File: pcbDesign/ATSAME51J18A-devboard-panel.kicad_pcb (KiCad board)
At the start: 2 copper layers, 100 x 100 mm, 294 parts, among them J1 Micro_SD_Card, J10 CAN, J11 Conn_01x32_Male, J2 BAT, J3 QWIIC, J7 Conn_01x32_Male, J9 USB4105_REVA, SW1 RST, U1 TCAN1051GVDRQ1, U2 ATSAME51J18A-A, U3 MIC5219-5.0YMM, U4 LM27762, U5 LM2775QDSGTQ1, U6 SC630AULTRT, U7 BQ24074RGT, U8 BQ27441DRZR-G1B, Y1 32.768

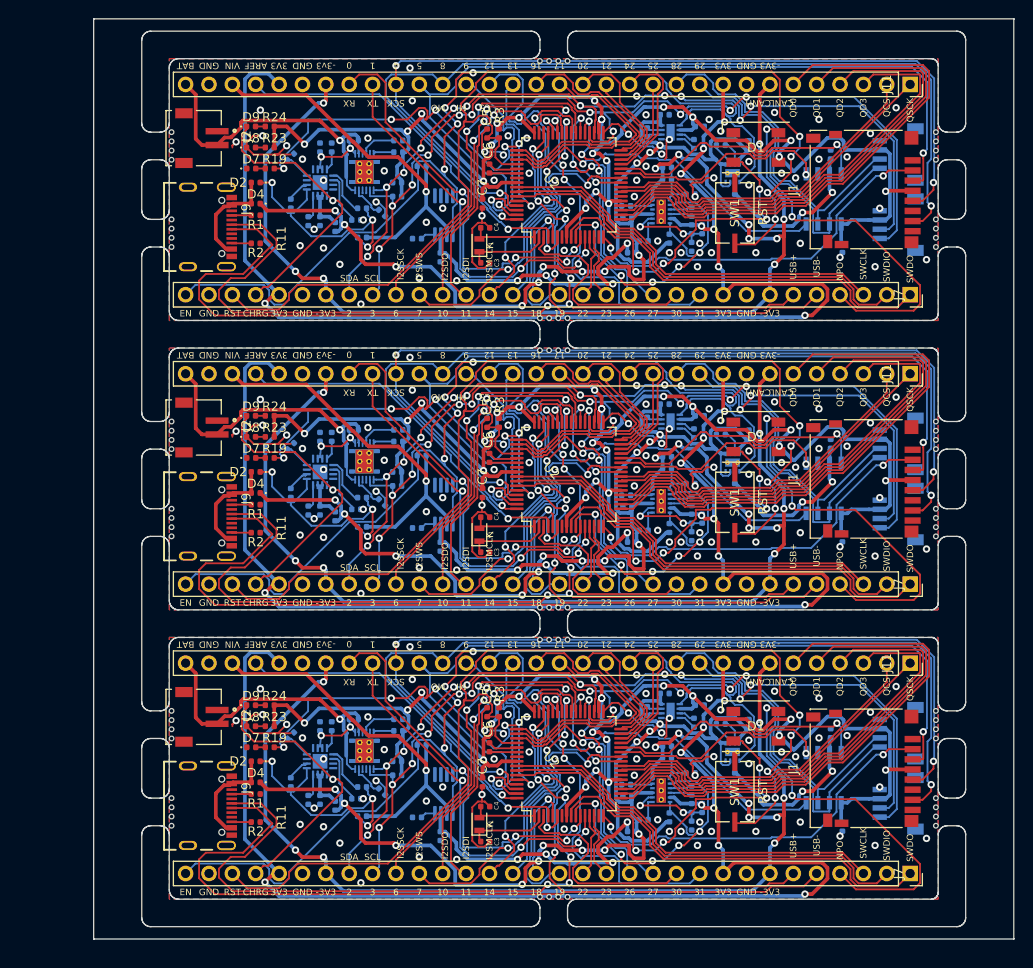
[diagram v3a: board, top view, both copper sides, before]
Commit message: Fixed panelizing issues
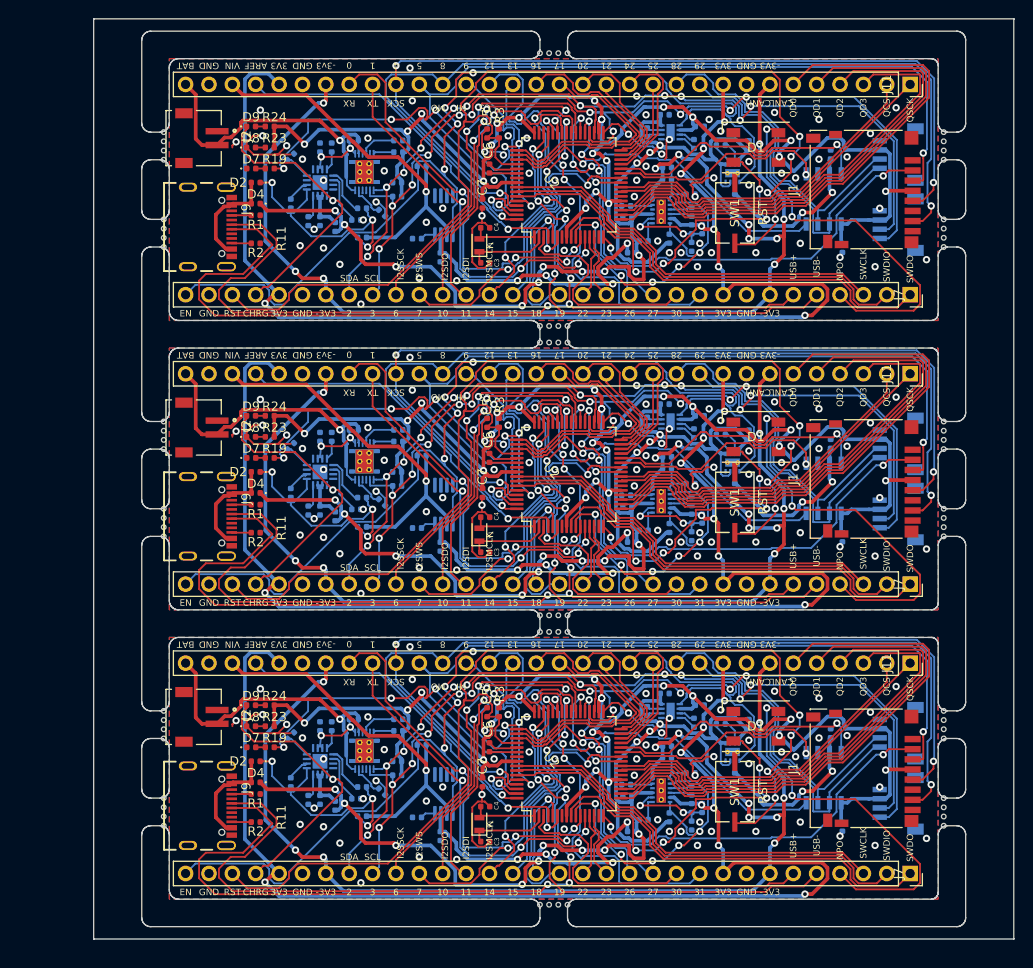
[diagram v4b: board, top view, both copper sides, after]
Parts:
- removed the D9 at (58.9, 120.3)
- removed the D9 at (58.9, 88.8)
- removed the D9 at (58.9, 57.4)
- removed the R24 at (60.9, 120.3)
- removed the R24 at (60.9, 88.8)
- removed the R24 at (60.9, 57.4)
- removed the REF** at (133.3, 133.4)
- removed the REF** at (50.2, 131.4)
- removed the REF** at (50.2, 132.4)
- removed the REF** at (50.2, 133.4)
- removed the REF** at (50.2, 120.9)
- removed the REF** at (50.2, 121.9)
- removed the REF** at (50.2, 122.9)
- removed the REF** at (50.2, 123.9)
- removed the REF** at (133.3, 101.9)
- removed the REF** at (133.3, 100.9)
- removed the REF** at (133.3, 99.9)
- removed the REF** at (133.3, 132.4)
- removed the REF** at (133.3, 98.9)
- removed the REF** at (133.3, 92.4)
- removed the REF** at (133.3, 91.4)
- removed the REF** at (133.3, 90.4)
- removed the REF** at (133.3, 89.4)
- removed the REF** at (50.2, 98.9)
- removed the REF** at (50.2, 99.9)
- removed the REF** at (50.2, 100.9)
- removed the REF** at (50.2, 101.9)
- removed the REF** at (50.2, 89.4)
- removed the REF** at (133.3, 131.4)
- removed the REF** at (50.2, 90.4)
- removed the REF** at (50.2, 91.4)
- removed the REF** at (50.2, 92.4)
- removed the REF** at (133.3, 70.5)
- removed the REF** at (133.3, 69.5)
- removed the REF** at (133.3, 68.5)
- removed the REF** at (133.3, 67.5)
- removed the REF** at (133.3, 61.0)
- removed the REF** at (133.3, 60.0)
- removed the REF** at (133.3, 59.0)
- removed the REF** at (133.3, 130.4)
- removed the REF** at (133.3, 58.0)
- removed the REF** at (50.2, 67.5)
- removed the REF** at (50.2, 68.5)
- removed the REF** at (50.2, 69.5)
- removed the REF** at (50.2, 70.5)
- removed the REF** at (50.2, 58.0)
- removed the REF** at (50.2, 59.0)
- removed the REF** at (50.2, 60.0)
- removed the REF** at (50.2, 61.0)
- removed the REF** at (90.3, 141.1)
- removed the REF** at (133.3, 123.9)
- removed the REF** at (91.3, 141.1)
- removed the REF** at (92.3, 141.1)
- removed the REF** at (93.3, 141.1)
- removed the REF** at (93.3, 113.1)
- removed the REF** at (92.3, 113.1)
- removed the REF** at (91.3, 113.1)
- removed the REF** at (90.3, 113.1)
- removed the REF** at (90.3, 109.6)
- removed the REF** at (91.3, 109.6)
- removed the REF** at (92.3, 109.6)
- removed the REF** at (133.3, 122.9)
- removed the REF** at (93.3, 109.6)
- removed the REF** at (93.3, 81.7)
- removed the REF** at (92.3, 81.7)
- removed the REF** at (91.3, 81.7)
- removed the REF** at (90.3, 81.7)
- removed the REF** at (90.3, 78.2)
- removed the REF** at (91.3, 78.2)
- removed the REF** at (92.3, 78.2)
- removed the REF** at (93.3, 78.2)
- removed the REF** at (93.3, 50.2)
- removed the REF** at (133.3, 121.9)
- removed the REF** at (92.3, 50.2)
- removed the REF** at (91.3, 50.2)
- removed the REF** at (90.3, 50.2)
- removed the REF** at (133.3, 120.9)
- removed the REF** at (50.2, 130.4)
- removed the U6 at (104.5, 120.9)
- removed the U6 at (104.5, 89.4)
- removed the U6 at (104.5, 58.0)
- added C23: 4.7u, Capacitor_SMD:C_0402_1005Metric, B.Cu at (66.4, 122.5)
- added C23: 4.7u, Capacitor_SMD:C_0402_1005Metric, B.Cu at (66.4, 91.1)
- added C23: 4.7u, Capacitor_SMD:C_0402_1005Metric, B.Cu at (66.4, 59.7)
- added R1: 5.1k, Resistor_SMD:R_0402_1005Metric, F.Cu at (59.4, 129.9)
- added R1: 5.1k, Resistor_SMD:R_0402_1005Metric, F.Cu at (59.4, 98.5)
- added R1: 5.1k, Resistor_SMD:R_0402_1005Metric, F.Cu at (59.4, 67.0)
- added R2: 5.1k, Resistor_SMD:R_0402_1005Metric, F.Cu at (59.4, 133.0)
- added R2: 5.1k, Resistor_SMD:R_0402_1005Metric, F.Cu at (59.4, 101.5)
- added R2: 5.1k, Resistor_SMD:R_0402_1005Metric, F.Cu at (59.4, 70.1)
- added REF**: NPTH, NPTH, F.Cu at (134.2, 130.4)
- added REF**: NPTH, NPTH, F.Cu at (49.4, 132.4)
- added REF**: NPTH, NPTH, F.Cu at (49.4, 131.4)
- added REF**: NPTH, NPTH, F.Cu at (49.4, 130.4)
- added REF**: NPTH, NPTH, F.Cu at (49.4, 123.9)
- added REF**: NPTH, NPTH, F.Cu at (49.4, 122.9)
- added REF**: NPTH, NPTH, F.Cu at (49.4, 121.9)
- added REF**: NPTH, NPTH, F.Cu at (49.4, 120.9)
- added REF**: NPTH, NPTH, F.Cu at (134.2, 98.9)
- added REF**: NPTH, NPTH, F.Cu at (134.2, 99.9)
- added REF**: NPTH, NPTH, F.Cu at (134.2, 100.9)
- added REF**: NPTH, NPTH, F.Cu at (134.2, 131.4)
- added REF**: NPTH, NPTH, F.Cu at (134.2, 101.9)
- added REF**: NPTH, NPTH, F.Cu at (134.2, 89.4)
- added REF**: NPTH, NPTH, F.Cu at (134.2, 90.4)
- added REF**: NPTH, NPTH, F.Cu at (134.2, 91.4)
- added REF**: NPTH, NPTH, F.Cu at (134.2, 92.4)
- added REF**: NPTH, NPTH, F.Cu at (49.4, 101.9)
- added REF**: NPTH, NPTH, F.Cu at (49.4, 100.9)
- added REF**: NPTH, NPTH, F.Cu at (49.4, 99.9)
- added REF**: NPTH, NPTH, F.Cu at (49.4, 98.9)
- added REF**: NPTH, NPTH, F.Cu at (49.4, 92.4)
- added REF**: NPTH, NPTH, F.Cu at (134.2, 132.4)
- added REF**: NPTH, NPTH, F.Cu at (49.4, 91.4)
- added REF**: NPTH, NPTH, F.Cu at (49.4, 90.4)
- added REF**: NPTH, NPTH, F.Cu at (49.4, 89.4)
- added REF**: NPTH, NPTH, F.Cu at (134.2, 67.5)
- added REF**: NPTH, NPTH, F.Cu at (134.2, 68.5)
- added REF**: NPTH, NPTH, F.Cu at (134.2, 69.5)
- added REF**: NPTH, NPTH, F.Cu at (134.2, 70.5)
- added REF**: NPTH, NPTH, F.Cu at (134.2, 58.0)
- added REF**: NPTH, NPTH, F.Cu at (134.2, 59.0)
- added REF**: NPTH, NPTH, F.Cu at (134.2, 60.0)
- added REF**: NPTH, NPTH, F.Cu at (134.2, 133.4)
- added REF**: NPTH, NPTH, F.Cu at (134.2, 61.0)
- added REF**: NPTH, NPTH, F.Cu at (49.4, 70.5)
- added REF**: NPTH, NPTH, F.Cu at (49.4, 69.5)
- added REF**: NPTH, NPTH, F.Cu at (49.4, 68.5)
- added REF**: NPTH, NPTH, F.Cu at (49.4, 67.5)
- added REF**: NPTH, NPTH, F.Cu at (49.4, 61.0)
- added REF**: NPTH, NPTH, F.Cu at (49.4, 60.0)
- added REF**: NPTH, NPTH, F.Cu at (49.4, 59.0)
- added REF**: NPTH, NPTH, F.Cu at (49.4, 58.0)
- added REF**: NPTH, NPTH, F.Cu at (93.3, 141.9)
- added REF**: NPTH, NPTH, F.Cu at (134.2, 120.9)
- added REF**: NPTH, NPTH, F.Cu at (92.3, 141.9)
- added REF**: NPTH, NPTH, F.Cu at (91.3, 141.9)
- added REF**: NPTH, NPTH, F.Cu at (90.3, 141.9)
- added REF**: NPTH, NPTH, F.Cu at (90.3, 112.3)
- added REF**: NPTH, NPTH, F.Cu at (91.3, 112.3)
- added REF**: NPTH, NPTH, F.Cu at (92.3, 112.3)
- added REF**: NPTH, NPTH, F.Cu at (93.3, 112.3)
- added REF**: NPTH, NPTH, F.Cu at (93.3, 110.5)
- added REF**: NPTH, NPTH, F.Cu at (92.3, 110.5)
- added REF**: NPTH, NPTH, F.Cu at (91.3, 110.5)
- added REF**: NPTH, NPTH, F.Cu at (134.2, 121.9)
- added REF**: NPTH, NPTH, F.Cu at (90.3, 110.5)
- added REF**: NPTH, NPTH, F.Cu at (90.3, 80.8)
- added REF**: NPTH, NPTH, F.Cu at (91.3, 80.8)
- added REF**: NPTH, NPTH, F.Cu at (92.3, 80.8)
- added REF**: NPTH, NPTH, F.Cu at (93.3, 80.8)
- added REF**: NPTH, NPTH, F.Cu at (93.3, 79.0)
- added REF**: NPTH, NPTH, F.Cu at (92.3, 79.0)
- added REF**: NPTH, NPTH, F.Cu at (91.3, 79.0)
- added REF**: NPTH, NPTH, F.Cu at (90.3, 79.0)
- added REF**: NPTH, NPTH, F.Cu at (90.3, 49.4)
- added REF**: NPTH, NPTH, F.Cu at (134.2, 122.9)
- added REF**: NPTH, NPTH, F.Cu at (91.3, 49.4)
- added REF**: NPTH, NPTH, F.Cu at (92.3, 49.4)
- added REF**: NPTH, NPTH, F.Cu at (93.3, 49.4)
- added REF**: NPTH, NPTH, F.Cu at (134.2, 123.9)
- added REF**: NPTH, NPTH, F.Cu at (49.4, 133.4)
- D9 (x3): renamed from R1; value 5.1k -> CHRG; footprint Resistor_SMD:R_0402_1005Metric -> LED_SMD:LED_0402_1005Metric
- R24 (x3): renamed from R2; value 5.1k -> 10k
- U6 (x3): renamed from C23; value 4.7u -> SC630AULTRT; footprint Capacitor_SMD:C_0402_1005Metric -> ul_SC630AULTRT:SC630AULTRT
- moved U6 38.1 mm to (104.5, 120.9), turned to 0 degrees
- moved U6 38.1 mm to (104.5, 89.4), turned to 0 degrees
- moved U6 38.1 mm to (104.5, 58.0), turned to 0 degrees
- moved R24 12.8 mm to (60.9, 120.3), turned to 180 degrees
- moved R24 12.8 mm to (60.9, 88.8), turned to 180 degrees
- moved R24 12.8 mm to (60.9, 57.4), turned to 180 degrees
- moved D9 9.67 mm to (58.9, 120.3), turned to 0 degrees
- moved D9 9.67 mm to (58.9, 88.8), turned to 0 degrees
- moved D9 9.67 mm to (58.9, 57.4), turned to 0 degrees
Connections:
- D9 pad 1: Board_3-GND -> Board_3-CHRG
- D9 pad 2: Board_3-Net-(J9-PadA5) -> Board_3-Net-(D9-Pad2)
- D9 pad 1: Board_2-GND -> Board_2-CHRG
- D9 pad 2: Board_2-Net-(J9-PadA5) -> Board_2-Net-(D9-Pad2)
- D9 pad 1: Board_1-GND -> Board_1-CHRG
- D9 pad 2: Board_1-Net-(J9-PadA5) -> Board_1-Net-(D9-Pad2)
- R24 pad 1: Board_3-Net-(J9-PadB5) -> Board_3-VBUS_3V3_CH0_REG
- R24 pad 2: Board_3-GND -> Board_3-Net-(D9-Pad2)
- R24 pad 1: Board_2-Net-(J9-PadB5) -> Board_2-VBUS_3V3_CH0_REG
- R24 pad 2: Board_2-GND -> Board_2-Net-(D9-Pad2)
- R24 pad 1: Board_1-Net-(J9-PadB5) -> Board_1-VBUS_3V3_CH0_REG
- R24 pad 2: Board_1-GND -> Board_1-Net-(D9-Pad2)
- U6 pad 1: Board_3-Net-(C23-Pad1) -> Board_3-GND
- U6 pad 2: Board_3-GND -> Board_3-Net-(C21-Pad2)
- U6 pad 1: Board_2-Net-(C23-Pad1) -> Board_2-GND
- U6 pad 2: Board_2-GND -> Board_2-Net-(C21-Pad2)
- U6 pad 1: Board_1-Net-(C23-Pad1) -> Board_1-GND
- U6 pad 2: Board_1-GND -> Board_1-Net-(C21-Pad2)

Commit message: Panelized
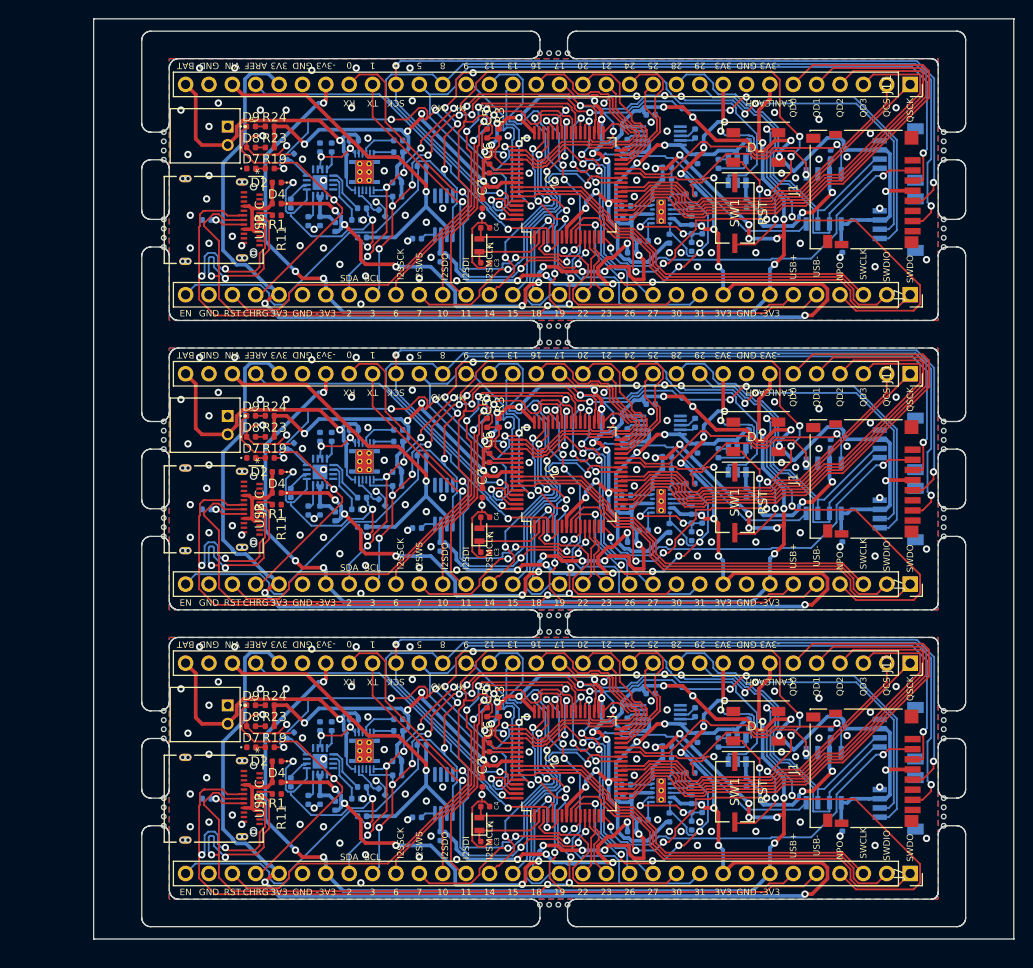
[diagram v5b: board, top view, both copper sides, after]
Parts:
- removed the C14 at (109.9, 122.3)
- removed the C14 at (109.9, 90.8)
- removed the C14 at (109.9, 59.4)
- removed the C17 at (107.0, 122.2)
- removed the C17 at (107.0, 90.7)
- removed the C17 at (107.0, 59.3)
- removed the C18 at (111.5, 128.1)
- removed the C18 at (111.5, 96.7)
- removed the C18 at (111.5, 65.2)
- removed the C19 at (107.7, 120.3)
- removed the C19 at (107.7, 88.8)
- removed the C19 at (107.7, 57.4)
- removed the C20 at (103.8, 119.0)
- removed the C20 at (103.8, 87.5)
- removed the C20 at (103.8, 56.1)
- removed the C21 at (101.9, 120.9)
- removed the C21 at (101.9, 89.4)
- removed the C21 at (101.9, 58.0)
- removed the D2 at (59.4, 126.4)
- removed the D2 at (59.4, 94.9)
- removed the D2 at (59.4, 63.5)
- removed the D4 at (59.4, 128.6)
- removed the D4 at (59.4, 97.2)
- removed the D4 at (59.4, 65.7)
- removed the J2 at (53.0, 121.5)
- removed the J2 at (53.0, 90.1)
- removed the J2 at (53.0, 58.6)
- removed J9 (x3): USB4105_REVA, USB4105_REVA:GCT_USB4105_REVA
- removed the R1 at (59.4, 129.9)
- removed the R1 at (59.4, 98.5)
- removed the R1 at (59.4, 67.0)
- removed the R2 at (59.4, 133.0)
- removed the R2 at (59.4, 101.5)
- removed the R2 at (59.4, 70.1)
- removed the U5 at (111.2, 125.3)
- removed the U5 at (111.2, 93.9)
- removed the U5 at (111.2, 62.4)
- removed U6 (x3): SC630AULTRT, ul_SC630AULTRT:SC630AULTRT
- added C14: 0.47u, Capacitor_SMD:C_0402_1005Metric, B.Cu at (109.7, 124.3)
- added C14: 0.47u, Capacitor_SMD:C_0402_1005Metric, B.Cu at (109.7, 92.9)
- added C14: 0.47u, Capacitor_SMD:C_0402_1005Metric, B.Cu at (109.7, 61.4)
- added C17: 1u, Capacitor_SMD:C_0402_1005Metric, B.Cu at (99.8, 122.2)
- added C17: 1u, Capacitor_SMD:C_0402_1005Metric, B.Cu at (99.8, 90.7)
- added C17: 1u, Capacitor_SMD:C_0402_1005Metric, B.Cu at (99.8, 59.3)
- added C18: 10u, Capacitor_SMD:C_0402_1005Metric, B.Cu at (112.7, 128.6)
- added C18: 10u, Capacitor_SMD:C_0402_1005Metric, B.Cu at (112.7, 97.2)
- added C18: 10u, Capacitor_SMD:C_0402_1005Metric, B.Cu at (112.7, 65.7)
- added C19: 4.7u, Capacitor_SMD:C_0402_1005Metric, B.Cu at (107.4, 123.8)
- added C19: 4.7u, Capacitor_SMD:C_0402_1005Metric, B.Cu at (107.4, 92.4)
- added C19: 4.7u, Capacitor_SMD:C_0402_1005Metric, B.Cu at (107.4, 60.9)
- added C20: 22u, Capacitor_SMD:C_0402_1005Metric, B.Cu at (102.3, 119.0)
- added C20: 22u, Capacitor_SMD:C_0402_1005Metric, B.Cu at (102.3, 87.5)
- added C20: 22u, Capacitor_SMD:C_0402_1005Metric, B.Cu at (102.3, 56.1)
- added C21: 1u, Capacitor_SMD:C_0402_1005Metric, B.Cu at (107.2, 121.0)
- added C21: 1u, Capacitor_SMD:C_0402_1005Metric, B.Cu at (107.2, 89.6)
- added C21: 1u, Capacitor_SMD:C_0402_1005Metric, B.Cu at (107.2, 58.1)
- added D2: D_Schottky, Diode_SMD:D_0402_1005Metric, F.Cu at (61.7, 126.4)
- added D2: D_Schottky, Diode_SMD:D_0402_1005Metric, F.Cu at (61.7, 94.9)
- added D2: D_Schottky, Diode_SMD:D_0402_1005Metric, F.Cu at (61.7, 63.5)
- added D4: D_Schottky, Diode_SMD:D_0402_1005Metric, F.Cu at (61.7, 128.6)
- added D4: D_Schottky, Diode_SMD:D_0402_1005Metric, F.Cu at (61.7, 97.2)
- added D4: D_Schottky, Diode_SMD:D_0402_1005Metric, F.Cu at (61.7, 65.7)
- added IC1: MP9361DJ-LF-P, SamacSys_Parts:SOT95P280X100-6N, B.Cu at (111.7, 125.1)
- added IC1: MP9361DJ-LF-P, SamacSys_Parts:SOT95P280X100-6N, B.Cu at (111.7, 93.6)
- added IC1: MP9361DJ-LF-P, SamacSys_Parts:SOT95P280X100-6N, B.Cu at (111.7, 62.2)
- added J2: USB C, usb_c:12401598E4-2A, F.Cu at (54.8, 130.4)
- added J2: USB C, usb_c:12401598E4-2A, F.Cu at (54.8, 99.0)
- added J2: USB C, usb_c:12401598E4-2A, F.Cu at (54.8, 67.5)
- added J4: S2B-PH-K-S(LF)(SN), S2B-PH-K-S_LF__SN_:JST_S2B-PH-K-S(LF)(SN), F.Cu at (56.4, 121.3)
- added J4: S2B-PH-K-S(LF)(SN), S2B-PH-K-S_LF__SN_:JST_S2B-PH-K-S(LF)(SN), F.Cu at (56.4, 89.8)
- added J4: S2B-PH-K-S(LF)(SN), S2B-PH-K-S_LF__SN_:JST_S2B-PH-K-S(LF)(SN), F.Cu at (56.4, 58.4)
- added R1: 5.1k, Resistor_SMD:R_0402_1005Metric, F.Cu at (61.7, 129.9)
- added R1: 5.1k, Resistor_SMD:R_0402_1005Metric, F.Cu at (61.7, 98.5)
- added R1: 5.1k, Resistor_SMD:R_0402_1005Metric, F.Cu at (61.7, 67.0)
- added R2: 5.1k, Resistor_SMD:R_0402_1005Metric, B.Cu at (54.1, 130.4)
- added R2: 5.1k, Resistor_SMD:R_0402_1005Metric, B.Cu at (54.1, 99.0)
- added R2: 5.1k, Resistor_SMD:R_0402_1005Metric, B.Cu at (54.1, 67.5)
- added U5: TPS60501DGS, Package_SO:MSOP-10_3x3mm_P0.5mm, B.Cu at (103.3, 121.3)
- added U5: TPS60501DGS, Package_SO:MSOP-10_3x3mm_P0.5mm, B.Cu at (103.3, 89.8)
- added U5: TPS60501DGS, Package_SO:MSOP-10_3x3mm_P0.5mm, B.Cu at (103.3, 58.4)
- C10 (x3): value 10u -> 2.2u
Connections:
- C10 pad 1: Board_3-GND -> Board_3-VBUS_NREG
- C10 pad 2: Board_3-VBUS_NREG -> Board_3-GND
- C10 pad 1: Board_2-GND -> Board_2-VBUS_NREG
- C10 pad 2: Board_2-VBUS_NREG -> Board_2-GND
- C10 pad 1: Board_1-GND -> Board_1-VBUS_NREG
- C10 pad 2: Board_1-VBUS_NREG -> Board_1-GND
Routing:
- net Board_1-VBUS_NREG: track 106.1 -> 88.2 mm, vias 12 -> 11
- net Board_3-VBUS_NREG: track 106.1 -> 88.2 mm, vias 12 -> 11
- net Board_2-VBUS_NREG: track 106.1 -> 88.2 mm, vias 12 -> 11
- net Board_3-USB_P: track 102.0 -> 117.9 mm, vias 6 -> 8
- net Board_2-USB_P: track 102.0 -> 117.9 mm, vias 6 -> 8
- net Board_1-USB_P: track 102.0 -> 117.9 mm, vias 6 -> 8
- net Board_2-USB_N: track 109.2 -> 122.9 mm, vias 4 -> 6
- net Board_3-USB_N: track 109.2 -> 122.9 mm, vias 4 -> 6
- net Board_1-USB_N: track 109.2 -> 122.9 mm, vias 4 -> 6
- net Board_1-EN: track 110.8 -> 102.8 mm
- net Board_2-EN: track 110.8 -> 102.8 mm
- net Board_3-EN: track 110.8 -> 102.8 mm
- net Board_3-VBUS_3V3_CH0_REG: track 170.1 -> 177.1 mm
- net Board_2-VBUS_3V3_CH0_REG: track 170.1 -> 177.1 mm
- net Board_1-VBUS_3V3_CH0_REG: track 170.1 -> 177.1 mm
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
